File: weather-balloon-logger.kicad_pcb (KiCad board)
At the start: 2 copper layers, 90 x 80 mm, 17 parts, among them J1 LightHAB VBATT/GND, J2 LightHABTracker 1.0, J3 LightHAB OUT1/GND, J5 Cutdown output

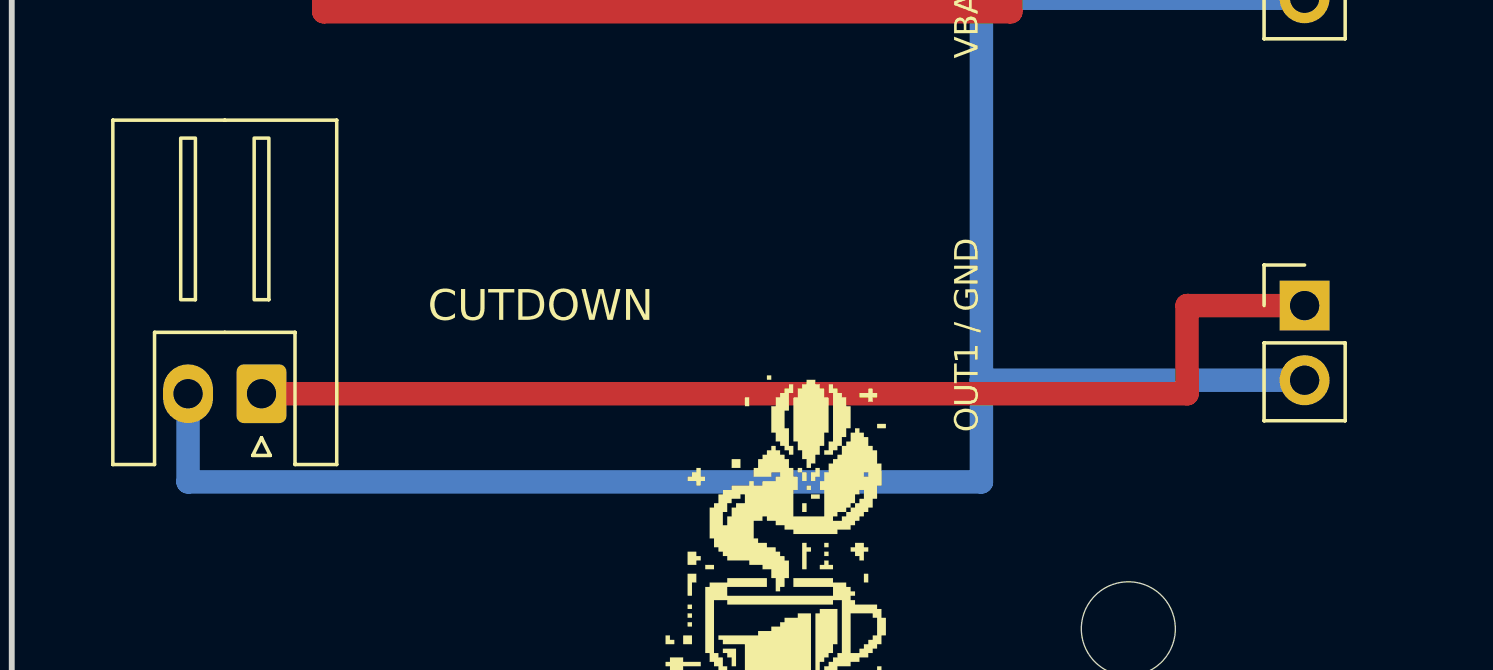
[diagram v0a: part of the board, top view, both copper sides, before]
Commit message: fix(pcb): route traces around logo
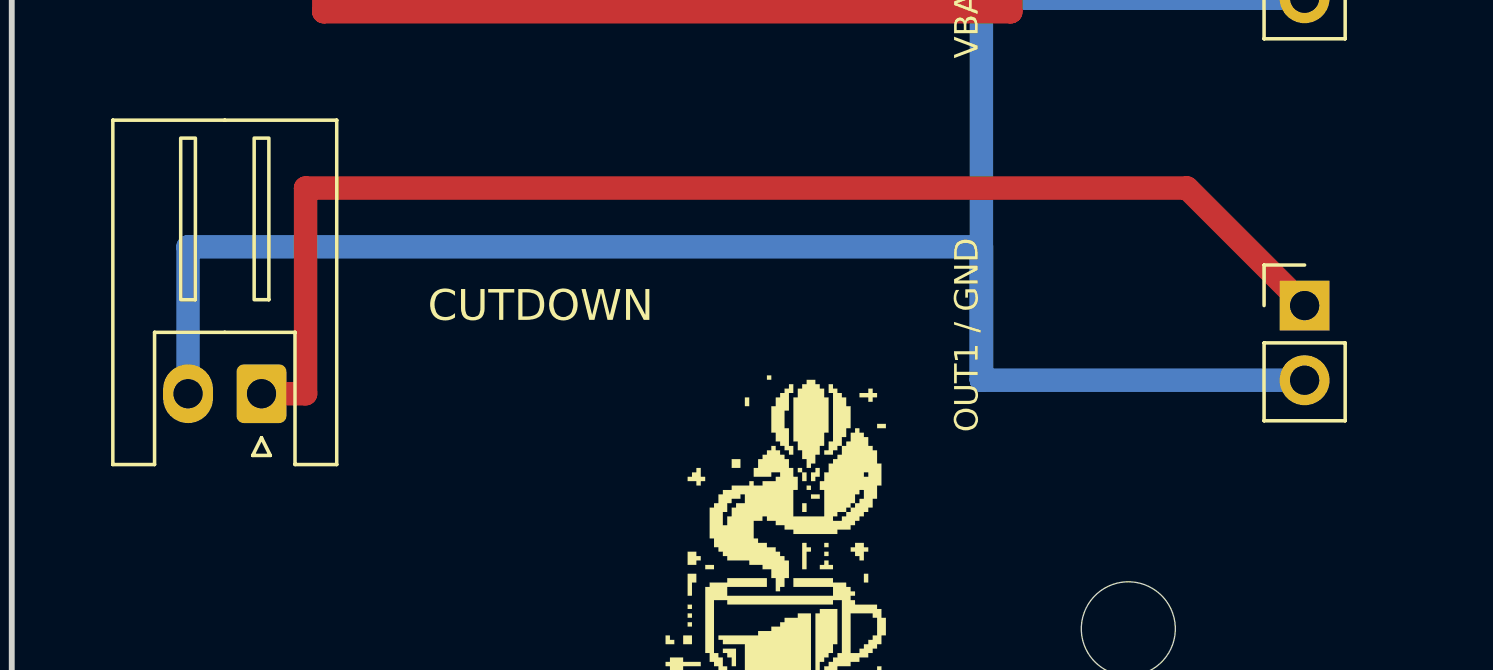
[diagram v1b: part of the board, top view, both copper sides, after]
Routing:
- net OUT1: track 38.5 -> 44.2 mm
- net GND: track 182.4 -> 185.5 mm

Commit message: refactor(power): use LightHAB 3V3 for OpenLog
Remove the separate VBATT-fed regulator path. Keep host rail capacity as a bench-test gate before fabrication.
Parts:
- removed A2: Pololu S7V8F5, Pololu_S7V8F5_Carrier
- removed J1: LightHAB VBATT/GND, PinHeader_1x02_P2.54mm_Vertical
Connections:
- A1 pad 3: LOGGER_5V -> 3V3
- C1 pad 1: LOGGER_5V -> 3V3
- C2 pad 1: LOGGER_5V -> 3V3
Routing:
- net 3V3: track 46.4 -> 124.6 mm
- net LOGGER_5V: track 70.4 -> 0.00 mm
- net VBATT: track 43.9 -> 0.00 mm
- net GND: track 185.5 -> 144.0 mm
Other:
- board text added: "LOGGER 3V3"
- board text removed: "LOGGER 5V"
- board text removed: "VBATT / GND"
